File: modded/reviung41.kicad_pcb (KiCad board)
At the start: 2 copper layers, 225.1 x 119 mm, 85 parts, among them SW10 SW_PUSH, SW11 SW_PUSH, SW12 SW_PUSH, SW14 SW_PUSH, SW15 SW_PUSH, SW16 SW_PUSH, SW17 SW_PUSH, SW18 SW_PUSH, SW19 SW_PUSH, SW2 SW_PUSH, SW20 SW_PUSH, SW21 SW_PUSH, SW22 SW_PUSH, SW23 SW_PUSH, SW25 SW_PUSH, SW26 SW_PUSH, SW27 SW_PUSH, SW28 SW_PUSH, SW29 SW_PUSH, SW3 SW_PUSH, SW31 SW_PUSH, SW32 SW_PUSH, SW33 SW_PUSH, SW34 SW_PUSH, SW35 SW_PUSH, SW37 SW_PUSH, SW38 SW_PUSH, SW39 SW_PUSH, SW4 SW_PUSH, SW40 SW_PUSH, SW41 SW_PUSH, SW42 SW_PUSH, SW5 SW_PUSH, SW6 SW_PUSH, SW8 SW_PUSH, SW9 SW_PUSH, U1 ProMicro

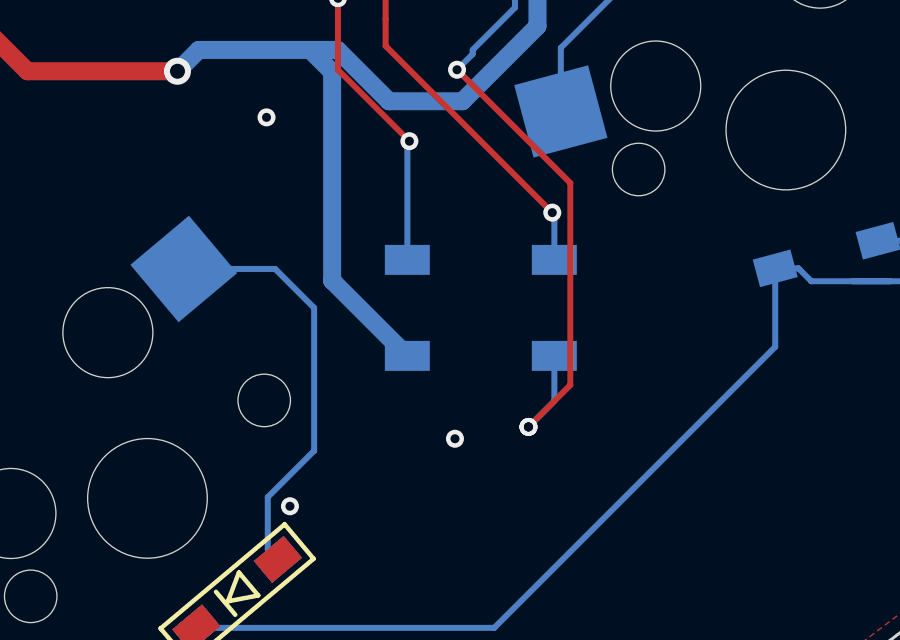
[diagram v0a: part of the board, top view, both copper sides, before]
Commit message: ever so slightly moved the bottom right led down
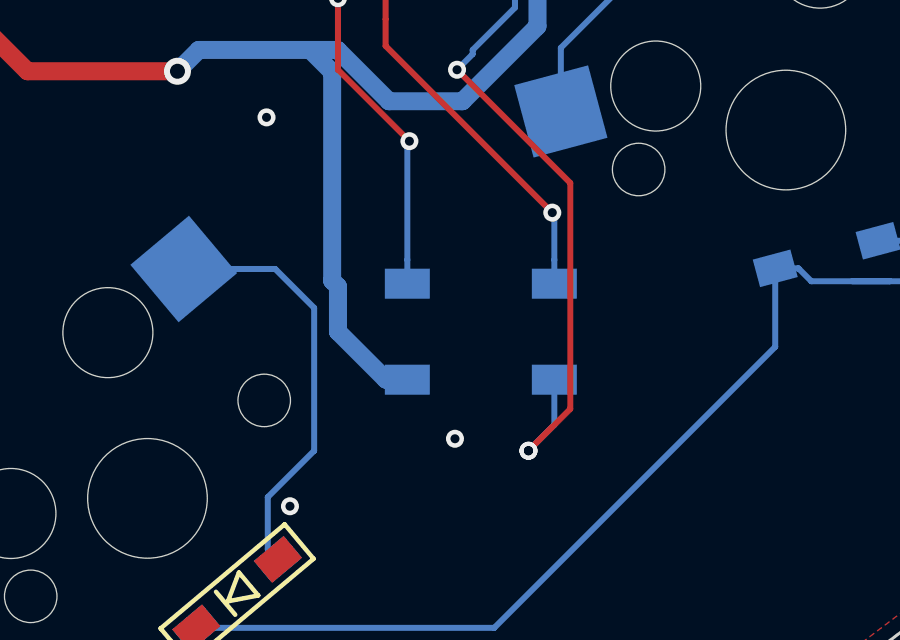
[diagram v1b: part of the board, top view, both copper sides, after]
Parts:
- moved L6 0.79 mm to (169.9, 148.4)
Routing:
- net GND: track 653.0 -> 654.2 mm
- net VCC: track 570.7 -> 571.5 mm
- net Net-(L6-Pad2): track 67.0 -> 67.8 mm
- net Net-(L5-Pad2): track 65.0 -> 65.8 mm
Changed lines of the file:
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@@
     (thickness 1.6)
     (drawings 766)
-    (tracks 1813)
+    (tracks 1818)
     (zones 0)
     (modules 85)
@@
   )
   (setup
-    (last_trace_width 0.254)
+    (last_trace_width 0.6)
     (user_trace_width 0.2)
     (user_trace_width 0.4)
@@
   )
   (module _reviung-kbd:LED_WS2812B_PLCC4_5.0x5.0mm_P3.2mm (layer B.Cu)
-    (at 169.8625 147.6375 180)
+    (at 169.8625 148.43125 180)
     (descr https://cdn-shop.adafruit.com/datasheets/WS2812B.pdf)
     (tags "LED RGB NeoPixel")
@@
   (via (at 166.6875 136.525) (size 0.6) (drill 0.3) (layers F.Cu B.Cu) (net 44))
   (segment (start 166.6875 136.525) (end 167.48125 135.73125) (width 0.2) (layer B.Cu) (net 44))
+  (segment (start 172.3125 146.0375) (end 172.3125 146.83125) (width 0.2) (layer B.Cu) (net 44))
   (segment (start 149.554539 61.67) (end 141.017894 53.133355) (width 0.6) (layer F.Cu) (net 45) (status 20))
   (segment (start 171.08 61.67) (end 149.554539 61.67) (width 0.6) (layer F.Cu) (net 45))
@@
   (segment (start 169.25 140.75) (end 171.75 138.25) (width 0.6) (layer B.Cu) (net 45))
   (segment (start 159.75 139.75) (end 160.46 139.04) (width 0.6) (layer B.Cu) (net 45))
-  (segment (start 164.906259 146.731259) (end 167.4125 149.2375) (width 0.6) (layer B.Cu) (net 45))
   (segment (start 164.906259 139.773759) (end 164.906259 146.731259) (width 0.6) (layer B.Cu) (net 45))
   (segment (start 160.46 139.04) (end 164.1725 139.04) (width 0.6) (layer B.Cu) (net 45))
   (segment (start 164.1725 139.04) (end 164.906259 139.773759) (width 0.6) (layer B.Cu) (net 45))
   (segment (start 164.1725 139.04) (end 165.09 139.04) (width 0.6) (layer B.Cu) (net 45))
+  (segment (start 167.4125 150.03125) (end 166.7 150.03125) (width 0.6) (layer B.Cu) (net 45))
+  (segment (start 166.7 150.03125) (end 165.1 148.43125) (width 0.6) (layer B.Cu) (net 45))
+  (segment (start 165.1 146.925) (end 164.906259 146.731259) (width 0.6) (layer B.Cu) (net 45))
+  (segment (start 165.1 148.43125) (end 165.1 146.925) (width 0.6) (layer B.Cu) (net 45))
   (segment (start 147.76013 55.218553) (end 147.76013 55.23987) (width 0.2) (layer B.Cu) (net 46))
   (segment (start 148.522129 54.456554) (end 147.76013 55.218553) (width 0.2) (layer B.Cu) (net 46) (status 10))
@@
   (segment (start 163.74 135.95875) (end 165.1 137.31875) (width 0.2) (layer B.Cu) (net 57))
   (segment (start 163.74 135.84) (end 163.74 135.95875) (width 0.2) (layer B.Cu) (net 57))
+  (segment (start 167.4125 146.0375) (end 167.4125 146.83125) (width 0.2) (layer B.Cu) (net 57))
   (segment (start 204.19 115.31) (end 208.29 115.31) (width 0.2) (layer B.Cu) (net 58))
   (segment (start 198.25 115.5) (end 204 115.5) (width 0.2) (layer B.Cu) (net 58))
@@
   (segment (start 184.5 122.75) (end 187.25 122.75) (width 0.2) (layer B.Cu) (net 58))
   (segment (start 187.25 122.75) (end 194.25 115.75) (width 0.2) (layer B.Cu) (net 58))
-  (segment (start 172.3125 149.2375) (end 172.3125 150.74375) (width 0.2) (layer B.Cu) (net 58))
-  (segment (start 172.3125 150.74375) (end 171.45 151.60625) (width 0.2) (layer B.Cu) (net 58))
-  (via (at 171.45 151.60625) (size 0.6) (drill 0.3) (layers F.Cu B.Cu) (net 58))
-  (via (at 171.45 151.60625) (size 0.6) (drill 0.3) (layers F.Cu B.Cu) (net 58))
-  (segment (start 172.843751 150.212499) (end 172.843751 143.475001) (width 0.2) (layer F.Cu) (net 58))
-  (segment (start 171.45 151.60625) (end 172.843751 150.212499) (width 0.2) (layer F.Cu) (net 58))
-  (segment (start 172.843751 143.475001) (end 169.06875 139.7) (width 0.2) (layer F.Cu) (net 58))
+  (via (at 171.45 152.4) (size 0.6) (drill 0.3) (layers F.Cu B.Cu) (net 58))
+  (via (at 171.45 152.4) (size 0.6) (drill 0.3) (layers F.Cu B.Cu) (net 58))
   (via (at 169.06875 139.7) (size 0.6) (drill 0.3) (layers F.Cu B.Cu) (net 58))
   (segment (start 169.59 139.17875) (end 169.59 139.04) (width 0.2) (layer B.Cu) (net 58))
   (segment (start 169.06875 139.7) (end 169.59 139.17875) (width 0.2) (layer B.Cu) (net 58))
+  (segment (start 172.3125 151.5375) (end 171.45 152.4) (width 0.2) (layer B.Cu) (net 58))
+  (segment (start 172.843751 143.475001) (end 169.06875 139.7) (width 0.2) (layer F.Cu) (net 58))
+  (segment (start 172.843751 151.006249) (end 172.843751 143.475001) (width 0.2) (layer F.Cu) (net 58))
+  (segment (start 171.45 152.4) (end 172.843751 151.006249) (width 0.2) (layer F.Cu) (net 58))
+  (segment (start 172.3125 151.5375) (end 172.3125 150.03125) (width 0.2) (layer B.Cu) (net 58))
   (segment (start 217.74 118.51) (end 213.19 118.51) (width 0.2) (layer B.Cu) (net 59))
   (segment (start 245.25 99.89) (end 247 101.64) (width 0.2) (layer B.Cu) (net 59))

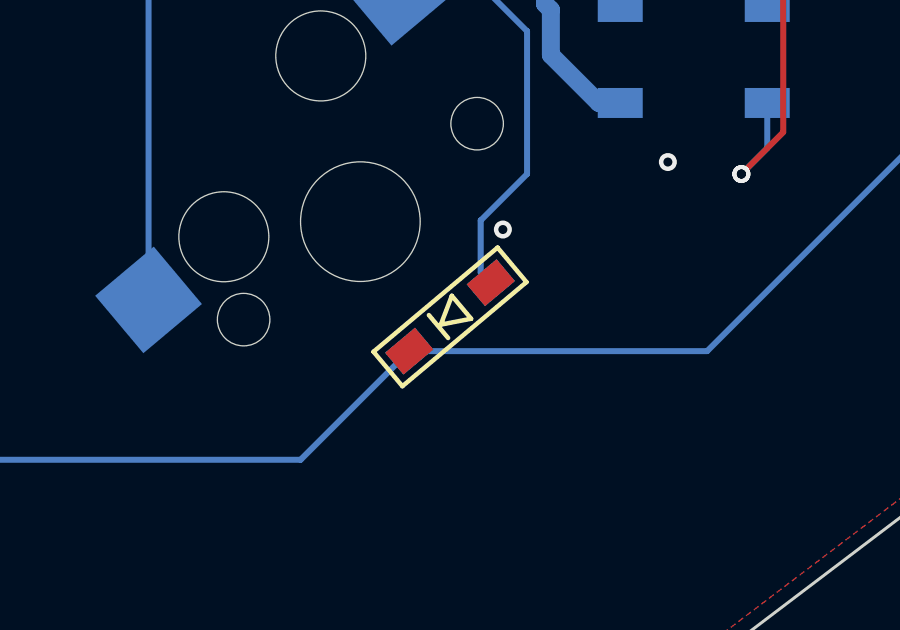
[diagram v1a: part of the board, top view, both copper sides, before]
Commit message: flipped the diode from the front to the back and aligned
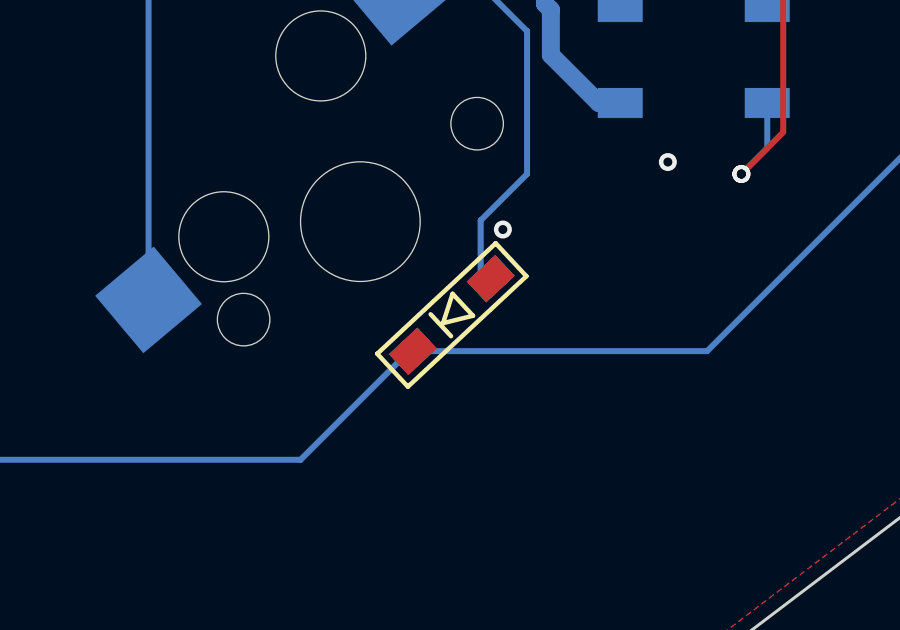
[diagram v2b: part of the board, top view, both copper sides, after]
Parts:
- D42: moved to B.Cu
- moved D42 0.09 mm to (161.8, 157.1), turned to 43 degrees
